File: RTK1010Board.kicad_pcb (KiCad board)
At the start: 2 copper layers, 56.2 x 53.3 mm, 53 parts, among them J1 SMA, J2 IPEX, J3 USB_OTG, U1 RTK-1010, U2 MCP1700-3002E_SOT23, U3 MCP1700-3002E_SOT23, U4 ESP32-S2-MINI-1

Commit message: gerber files added
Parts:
- moved C2 0.67 mm to (193.7, 101.6)
- moved R14 0.64 mm to (189.7, 101.6)
- moved R13 0.63 mm to (189.7, 104.8)
- moved C3 0.62 mm to (193.5, 104.8)
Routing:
- net Net-(C2-Pad2): track 36.1 -> 36.9 mm
- net Net-(C3-Pad2): track 32.6 -> 32.0 mm
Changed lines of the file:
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@@
       (drillshape 0)
       (scaleselection 1)
-      (outputdirectory "out")
+      (outputdirectory "gerber")
     )
   )
@@
   )
   (footprint "Capacitor_SMD:C_0805_2012Metric_Pad1.18x1.45mm_HandSolder" (layer "B.Cu")
-    (at 193.450076 104.151857 180)
+    (at 193.450076 104.775 180)
     (descr "Capacitor SMD 0805 (2012 Metric), square (rectangular) end terminal, IPC_7351 nominal with elongated pad for handsoldering. (Body size source: IPC-SM-782 page 76, https://www.pcb-3d.com/wordpress/wp-content/uploads/ipc-sm-782a_amendment_1_and_2.pdf, https://docs.google.com/spreadsheets/d/1BsfQQcO9C6DZCsRaXUlFlo91Tg2WpOkGARC1WS5S8t0/edit?usp=sharing), generated with kicad-footprint-generator")
     (tags "capacitor handsolder")
@@
   )
   (footprint "Capacitor_SMD:C_0805_2012Metric_Pad1.18x1.45mm_HandSolder" (layer "B.Cu")
-    (at 193.4425 102.225 180)
+    (at 193.675 101.6 180)
     (descr "Capacitor SMD 0805 (2012 Metric), square (rectangular) end terminal, IPC_7351 nominal with elongated pad for handsoldering. (Body size source: IPC-SM-782 page 76, https://www.pcb-3d.com/wordpress/wp-content/uploads/ipc-sm-782a_amendment_1_and_2.pdf, https://docs.google.com/spreadsheets/d/1BsfQQcO9C6DZCsRaXUlFlo91Tg2WpOkGARC1WS5S8t0/edit?usp=sharing), generated with kicad-footprint-generator")
     (tags "capacitor handsolder")
@@
   )
   (footprint "Resistor_SMD:R_0805_2012Metric_Pad1.20x1.40mm_HandSolder" (layer "B.Cu")
-    (at 189.717131 104.141605 180)
+    (at 189.717131 104.775 180)
     (descr "Resistor SMD 0805 (2012 Metric), square (rectangular) end terminal, IPC_7351 nominal with elongated pad for handsoldering. (Body size source: IPC-SM-782 page 72, https://www.pcb-3d.com/wordpress/wp-content/uploads/ipc-sm-782a_amendment_1_and_2.pdf), generated with kicad-footprint-generator")
     (tags "resistor handsolder")
@@
   )
   (footprint "Resistor_SMD:R_0805_2012Metric_Pad1.20x1.40mm_HandSolder" (layer "B.Cu")
-    (at 189.717131 102.236605 180)
+    (at 189.717131 101.6 180)
     (descr "Resistor SMD 0805 (2012 Metric), square (rectangular) end terminal, IPC_7351 nominal with elongated pad for handsoldering. (Body size source: IPC-SM-782 page 72, https://www.pcb-3d.com/wordpress/wp-content/uploads/ipc-sm-782a_amendment_1_and_2.pdf), generated with kicad-footprint-generator")
     (tags "resistor handsolder")
@@
   (segment (start 189.564 122.555) (end 189.4445 122.6745) (width 0.25) (layer "B.Cu") (net 25))
   (segment (start 193.04 97.155) (end 194.31 95.885) (width 0.25) (layer "B.Cu") (net 25))
+  (segment (start 183.066396 121.1) (end 182.376396 121.79) (width 0.25) (layer "B.Cu") (net 30))
+  (segment (start 188.41 113.852792) (end 188.41 120.201396) (width 0.25) (layer "B.Cu") (net 30))
+  (segment (start 193.575076 108.687716) (end 188.41 113.852792) (width 0.25) (layer "B.Cu") (net 30))
+  (segment (start 188.41 120.201396) (end 187.511396 121.1) (width 0.25) (layer "B.Cu") (net 30))
+  (segment (start 190.717131 101.6) (end 192.6375 101.6) (width 0.25) (layer "B.Cu") (net 30))
+  (segment (start 192.6375 101.6) (end 193.575076 102.537576) (width 0.25) (layer "B.Cu") (net 30))
+  (segment (start 187.511396 121.1) (end 183.066396 121.1) (width 0.25) (layer "B.Cu") (net 30))
+  (segment (start 193.575076 102.537576) (end 193.575076 108.687716) (width 0.25) (layer "B.Cu") (net 30))
+  (segment (start 176.875837 122.929441) (end 175.698297 122.929441) (width 0.25) (layer "B.Cu") (net 30))
+  (segment (start 178.015278 121.79) (end 176.875837 122.929441) (width 0.25) (layer "B.Cu") (net 30))
   (segment (start 182.376396 121.79) (end 178.015278 121.79) (width 0.25) (layer "B.Cu") (net 30))
-  (segment (start 188.41 113.852792) (end 188.41 120.201396) (width 0.25) (layer "B.Cu") (net 30))
-  (segment (start 190.717131 102.236605) (end 192.393395 102.236605) (width 0.25) (layer "B.Cu") (net 30))
-  (segment (start 193.575076 108.687716) (end 188.41 113.852792) (width 0.25) (layer "B.Cu") (net 30))
-  (segment (start 183.066396 121.1) (end 182.376396 121.79) (width 0.25) (layer "B.Cu") (net 30))
-  (segment (start 188.41 120.201396) (end 187.511396 121.1) (width 0.25) (layer "B.Cu") (net 30))
-  (segment (start 187.511396 121.1) (end 183.066396 121.1) (width 0.25) (layer "B.Cu") (net 30))
-  (segment (start 178.015278 121.79) (end 176.875837 122.929441) (width 0.25) (layer "B.Cu") (net 30))
-  (segment (start 192.393395 102.236605) (end 192.405 102.225) (width 0.25) (layer "B.Cu") (net 30))
-  (segment (start 176.875837 122.929441) (end 175.698297 122.929441) (width 0.25) (layer "B.Cu") (net 30))
-  (segment (start 192.405 102.225) (end 193.575076 103.395076) (width 0.25) (layer "B.Cu") (net 30))
-  (segment (start 193.575076 103.395076) (end 193.575076 108.687716) (width 0.25) (layer "B.Cu") (net 30))
   (segment (start 207.6 120.09) (end 207.04 120.65) (width 0.25) (layer "B.Cu") (net 31))
   (segment (start 212.09 120.09) (end 207.6 120.09) (width 0.25) (layer "B.Cu") (net 31))
-  (segment (start 187.325 120.65) (end 187.96 120.015) (width 0.25) (layer "B.Cu") (net 32))
-  (segment (start 182.19 121.34) (end 182.88 120.65) (width 0.25) (layer "B.Cu") (net 32))
-  (segment (start 192.402324 104.141605) (end 192.412576 104.151857) (width 0.25) (layer "B.Cu") (net 32))
-  (segment (start 192.412576 109.21382) (end 192.412576 104.151857) (width 0.25) (layer "B.Cu") (net 32))
-  (segment (start 187.96 113.666396) (end 192.412576 109.21382) (width 0.25) (layer "B.Cu") (net 32))
-  (segment (start 187.96 120.015) (end 187.96 113.666396) (width 0.25) (layer "B.Cu") (net 32))
-  (segment (start 190.717131 104.141605) (end 192.402324 104.141605) (width 0.25) (layer "B.Cu") (net 32))
-  (segment (start 182.88 120.65) (end 187.325 120.65) (width 0.25) (layer "B.Cu") (net 32))
-  (segment (start 177.886167 121.34) (end 182.19 121.34) (width 0.25) (layer "B.Cu") (net 32))
-  (segment (start 175.698297 122.279441) (end 176.889441 122.279441) (width 0.25) (layer "B.Cu") (net 32))
-  (segment (start 177.857525 121.311357) (end 177.886167 121.34) (width 0.25) (layer "B.Cu") (net 32))
-  (segment (start 176.889441 122.279441) (end 177.857525 121.311357) (width 0.25) (layer "B.Cu") (net 32))
+  (segment (start 176.889441 122.279441) (end 175.698297 122.279441) (width 0.25) (layer "B.Cu") (net 32))
+  (segment (start 187.96 120.015) (end 187.325 120.65) (width 0.25) (layer "B.Cu") (net 32))
+  (segment (start 192.412576 109.21382) (end 187.96 113.666396) (width 0.25) (layer "B.Cu") (net 32))
+  (segment (start 190.717131 104.775) (end 192.412576 104.775) (width 0.25) (layer "B.Cu") (net 32))
+  (segment (start 187.96 113.666396) (end 187.96 120.015) (width 0.25) (layer "B.Cu") (net 32))
+  (segment (start 182.19 121.34) (end 177.886167 121.34) (width 0.25) (layer "B.Cu") (net 32))
+  (segment (start 192.412576 104.775) (end 192.412576 109.21382) (width 0.25) (layer "B.Cu") (net 32))
+  (segment (start 177.857525 121.311357) (end 176.889441 122.279441) (width 0.25) (layer "B.Cu") (net 32))
+  (segment (start 177.886167 121.34) (end 177.857525 121.311357) (width 0.25) (layer "B.Cu") (net 32))
+  (segment (start 182.88 120.65) (end 182.19 121.34) (width 0.25) (layer "B.Cu") (net 32))
+  (segment (start 187.325 120.65) (end 182.88 120.65) (width 0.25) (layer "B.Cu") (net 32))
   (segment (start 198.460001 110.49) (end 198.460001 119.039999) (width 0.25) (layer "B.Cu") (net 33))
   (segment (start 202.375015 94.061036) (end 199.478297 96.957754) (width 0.25) (layer "B.Cu") (net 33))

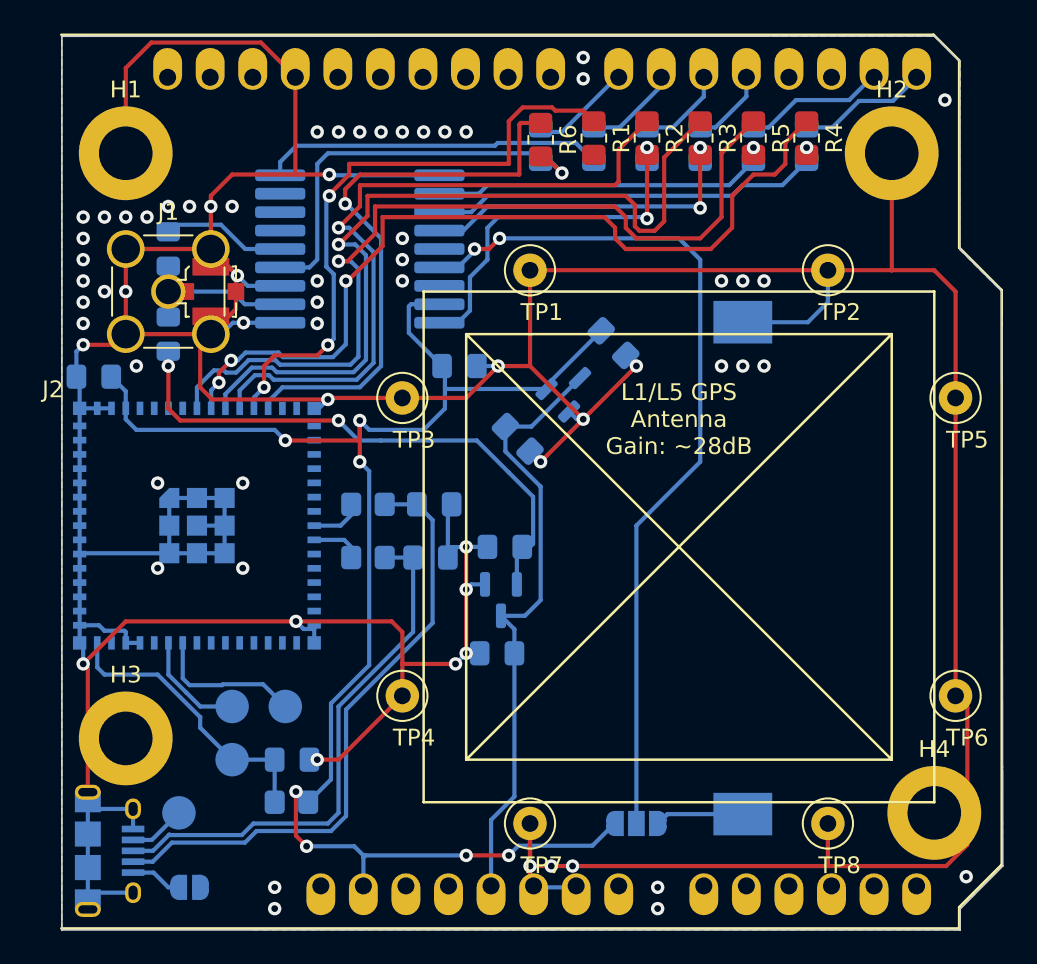
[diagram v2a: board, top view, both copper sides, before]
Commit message: ESP32-S2 mini replaced by WROVER module
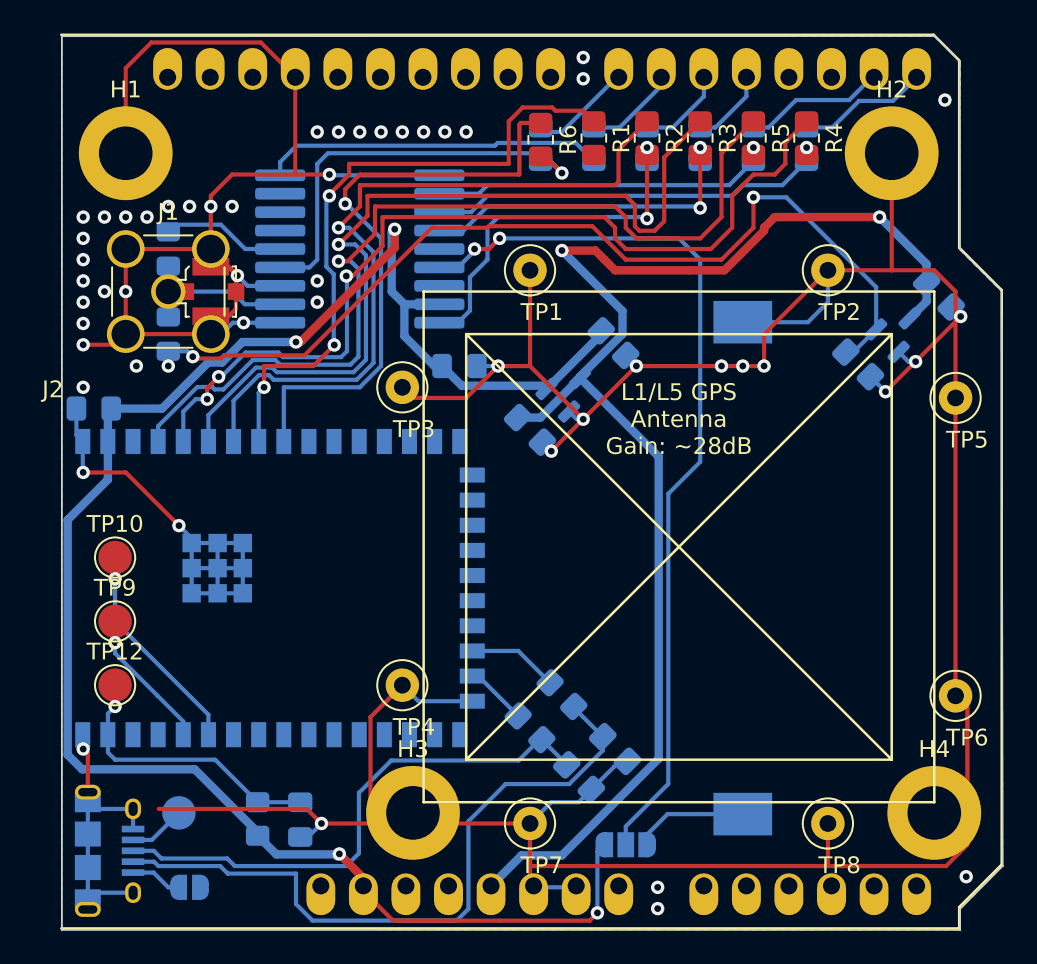
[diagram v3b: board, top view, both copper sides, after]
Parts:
- TP10, TP12, TP9: moved to F.Cu
- U4: value ESP32-S2-MINI-1 -> ESP32-S2-WROVER; footprint Espressif:ESP32-S2-MINI-1 -> Espressif:ESP32-S2-WROVER
- moved C6 34.0 mm to (223.8, 89.1), turned to -45 degrees
- moved U3 28.7 mm to (221.4, 91.2), turned to 45 degrees
- moved C7 23.7 mm to (219.0, 93.2), turned to -45 degrees
- moved C2 18.2 mm to (204.5, 116.2), turned to 135 degrees
- moved H3 17.7 mm to (192.4, 120.0)
- moved R14 16.2 mm to (201.3, 113.0), turned to 135 degrees
- moved C3 15.8 mm to (202.3, 117.9), turned to 135 degrees
- moved R13 14.0 mm to (199.4, 114.9), turned to 135 degrees
- moved TP10 13.5 mm to (174.6, 104.8), turned to 0 degrees
- moved TP9 8.64 mm to (174.6, 108.6), turned to 0 degrees
- moved TP12 8.28 mm to (174.6, 112.4), turned to 0 degrees
- moved U4 5.72 mm to (183.8, 106.6)
- moved C9 3.61 mm to (185.7, 120.4), turned to 90 degrees
- moved R15 2.25 mm to (183.1, 120.4), turned to -90 degrees
- moved C8 1.91 mm to (173.4, 95.9)
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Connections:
- JP2 pad 2: 5V -> unconnected-(JP2-Pad2)
- U4 pad 10: Net-(R3-Pad1) -> unconnected-(U4-Pad10)
- U4 pad 11: Net-(R2-Pad1) -> unconnected-(U4-Pad11)
- U4 pad 12: Net-(R1-Pad1) -> unconnected-(U4-Pad12)
- U4 pad 13: Net-(R6-Pad1) -> unconnected-(U4-Pad13)
- U4 pad 2: GND -> +3V3
- U4 pad 23: Net-(R14-Pad2) -> unconnected-(U4-Pad23)
- U4 pad 24: Net-(R13-Pad2) -> Net-(R14-Pad2)
- U4 pad 25: unconnected-(U4-Pad25) -> Net-(R13-Pad2)
- U4 pad 26: unconnected-(U4-Pad26) -> GND
- U4 pad 3: +3V3 -> unconnected-(U4-Pad3)
- U4 pad 30: GND -> unconnected-(U4-Pad30)
- U4 pad 37: unconnected-(U4-Pad37) -> Net-(TP10-Pad1)
- U4 pad 38: unconnected-(U4-Pad38) -> Net-(TP9-Pad1)
- U4 pad 39: Net-(TP10-Pad1) -> unconnected-(U4-Pad39)
- U4 pad 4: unconnected-(U4-Pad4) -> Net-(R5-Pad1)
- U4 pad 40: Net-(TP9-Pad1) -> unconnected-(U4-Pad40)
- U4 pad 41: unconnected-(U4-Pad41) -> Net-(C9-Pad2)
- U4 pad 5: unconnected-(U4-Pad5) -> Net-(R4-Pad1)
- U4 pad 6: unconnected-(U4-Pad6) -> Net-(R3-Pad1)
- U4 pad 7: unconnected-(U4-Pad7) -> Net-(R2-Pad1)
- U4 pad 8: Net-(R5-Pad1) -> Net-(R1-Pad1)
- U4 pad 9: Net-(R4-Pad1) -> Net-(R6-Pad1)
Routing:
- net U5: track 36.7 -> 81.2 mm, vias 0 -> 2
- net GND: track 350.6 -> 319.0 mm, vias 67 -> 51
- net Net-(C7-Pad1): track 33.3 -> 57.6 mm, vias 2 -> 3
- net +3V3: track 94.4 -> 108.9 mm, vias 7 -> 4
- net Net-(C2-Pad2): track 36.9 -> 41.2 mm
- net Net-(TP10-Pad1): track 8.98 -> 12.9 mm, vias 0 -> 1
- net Net-(R4-Pad1): track 50.9 -> 54.3 mm
- net Net-(R14-Pad2): track 2.47 -> 5.43 mm
- net Net-(R5-Pad1): track 52.0 -> 54.9 mm
- net Net-(R3-Pad1): track 48.5 -> 50.8 mm
- net Net-(R1-Pad1): track 36.6 -> 38.7 mm
- net Net-(R2-Pad1): track 42.2 -> 44.2 mm
- net Net-(TP9-Pad1): track 6.49 -> 8.45 mm, vias 0 -> 1
- net Net-(R13-Pad2): track 2.38 -> 4.15 mm
- net Net-(R6-Pad1): track 34.6 -> 36.1 mm
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
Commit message: gerber files created
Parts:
- moved C8 0.38 mm to (173.4, 95.5)
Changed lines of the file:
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@@
       (drillshape 0)
       (scaleselection 1)
-      (outputdirectory "out")
+      (outputdirectory "gerber")
     )
   )
@@
       (net 35 "EN") (pinfunction "D5") (pintype "bidirectional+no_connect"))
     (pad "D6" thru_hole oval (at 35.814 -50.8) (size 1.7272 2.5) (drill 1.016 (offset 0 -0.5)) (layers *.Cu *.Mask)
-      (net 36 "GPIO26") (pinfunction "D6") (pintype "bidirectional+no_connect"))
+      (net 36 "GPIO26") (pinfunction "D6") (pintype "bidirectional"))
     (pad "D7" thru_hole oval (at 33.274 -50.8) (size 1.7272 2.5) (drill 1.016 (offset 0 -0.5)) (layers *.Cu *.Mask)
       (net 37 "LNA_EN") (pinfunction "D7") (pintype "bidirectional"))
@@
       (net 43 "_GPIO26") (pintype "passive"))
     (pad "2" smd roundrect (at 1 0 90) (size 1.2 1.4) (layers "B.Cu" "B.Paste" "B.Mask") (roundrect_rratio 0.2083333333)
-      (net 36 "GPIO26") (pintype "passive+no_connect"))
+      (net 36 "GPIO26") (pintype "passive"))
     (model "${KICAD6_3DMODEL_DIR}/Resistor_SMD.3dshapes/R_0805_2012Metric.wrl"
       (offset (xyz 0 0 0))
@@
   )
   (footprint "Capacitor_SMD:C_0805_2012Metric_Pad1.18x1.45mm_HandSolder" (layer "B.Cu")
-    (at 173.355 95.885 180)
+    (at 173.355 95.504 180)
     (descr "Capacitor SMD 0805 (2012 Metric), square (rectangular) end terminal, IPC_7351 nominal with elongated pad for handsoldering. (Body size source: IPC-SM-782 page 76, https://www.pcb-3d.com/wordpress/wp-content/uploads/ipc-sm-782a_amendment_1_and_2.pdf, https://docs.google.com/spreadsheets/d/1BsfQQcO9C6DZCsRaXUlFlo91Tg2WpOkGARC1WS5S8t0/edit?usp=sharing), generated with kicad-footprint-generator")
     (tags "capacitor handsolder")

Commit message: some more small changes
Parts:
- added C10: 10uF, Capacitor_Tantalum_SMD:CP_EIA-7132-20_AVX-U_Pad2.72x3.50mm_HandSolder, B.Cu at (225.3, 104.8)
- added C11: 10uF, Capacitor_Tantalum_SMD:CP_EIA-7132-20_AVX-U_Pad2.72x3.50mm_HandSolder, B.Cu at (199.9, 104.5)
- BT1: value Battery_Cell -> 3.3V
- JP2: value Jumper_2_Open -> USB power
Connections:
- net Net-(C7-Pad1) renamed ULNA
- JP2 pad 2: unconnected-(JP2-Pad2) -> 5V
- R11 pad 2: _PPS -> Net-(R11-Pad2)
- U1 pad 4: _PPS -> Net-(R11-Pad2)
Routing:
- net _PPS: track 21.0 -> 0.00 mm, vias 2 -> 0
- net Net-(R11-Pad2): track 0.00 -> 21.0 mm, vias 0 -> 2
- net GND: track 319.0 -> 335.6 mm, vias 51 -> 52
- net ULNA: track 57.6 -> 72.0 mm
- net +3V3: track 108.9 -> 117.5 mm

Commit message: -
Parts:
- added TP_GND1: TestPoint, TestPoint:TestPoint_Pad_D2.0mm, F.Cu at (174.5, 101.1)
- renumbered TP12 to TP_EN1, TP11 to TP_OTG1, TP9 to TP_U0RXD1, TP10 to TP_U0TXD1
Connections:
- net EN renamed Net-(R12-Pad1)
- net GPIO26 renamed Net-(R10-Pad2)
- net LNA_EN renamed Net-(R9-Pad2)
- net PPS renamed Net-(R11-Pad1)
- R11 pad 2: Net-(R11-Pad2) -> _PPS
- U1 pad 4: Net-(R11-Pad2) -> _PPS
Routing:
- net Net-(R11-Pad2): track 21.0 -> 0.00 mm, vias 2 -> 0
- net _PPS: track 0.00 -> 20.3 mm, vias 0 -> 2
- net U5: track 81.2 -> 83.8 mm
- net +3V3: track 117.5 -> 118.4 mm
- net ULNA: track 72.0 -> 71.3 mm
- net Net-(R5-Pad1): track 54.9 -> 54.3 mm
